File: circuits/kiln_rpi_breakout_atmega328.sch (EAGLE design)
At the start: 31 parts, among them Q1 5A, U1 INA125P

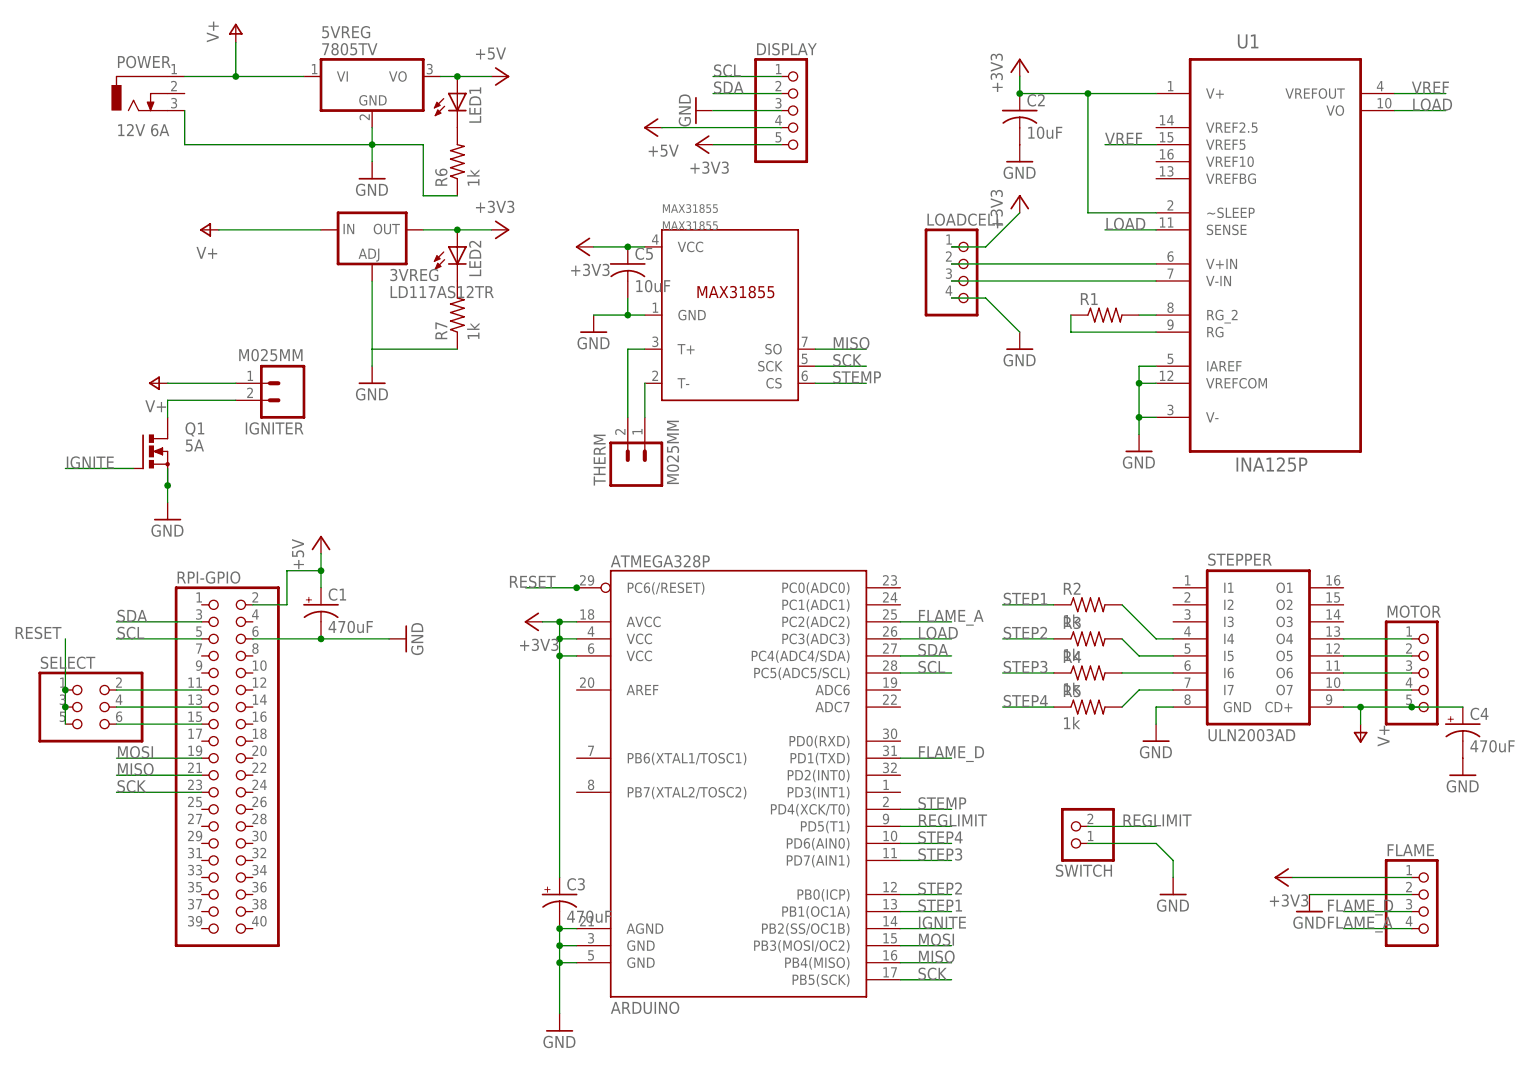
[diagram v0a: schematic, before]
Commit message: Add auxtemp header, stacking power connector
Managed to update the pcb order in time. Auxtemp header takes a DS18B20
chip as an auxiliary temperature monitor, good for checking for propane
tank freezing or even as primary temperature control. Additional
powerstack header allows stacked breakouts to pass power between boards
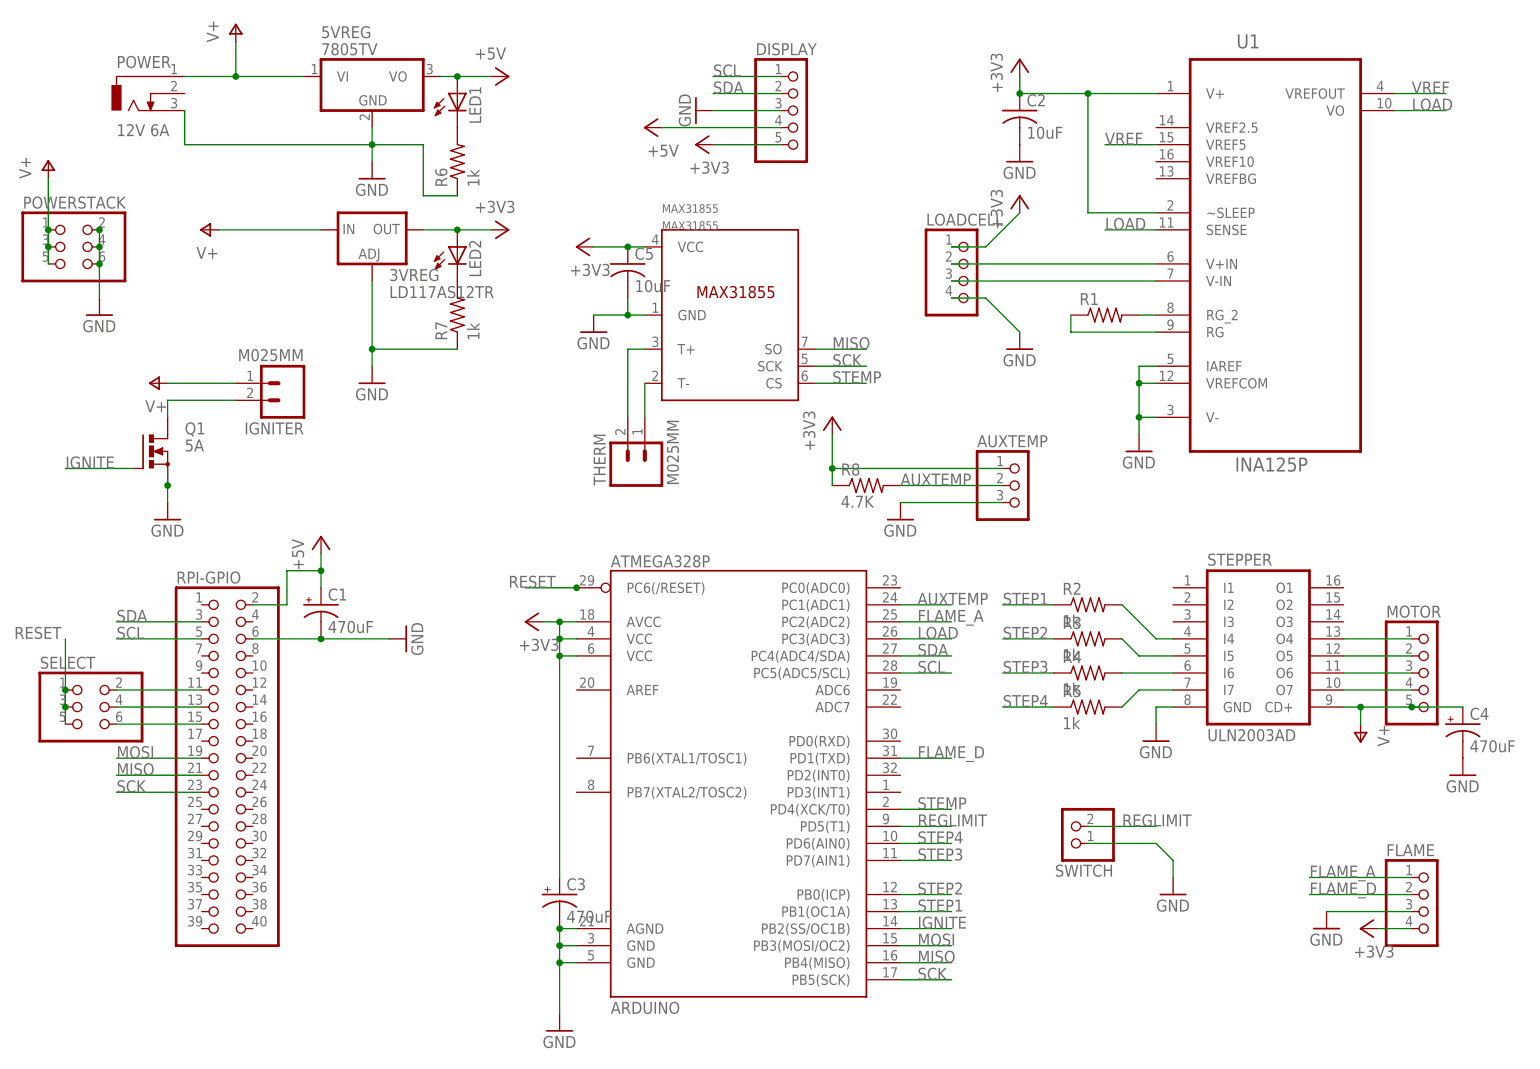
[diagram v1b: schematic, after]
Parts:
- added AUXTEMP: (no value), pinhead:PINHD-1X3
- added POWERSTACK: (no value), pinhead:PINHD-2X3
- added R8: 4.7K, rcl:R-US_0207/2V
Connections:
- new net AUXTEMP: ARDUINO.PC1(ADC1), AUXTEMP.2, R8.2
- net +3V3: now also AUXTEMP.1, FLAME.4, R8.1; no longer FLAME.1
- net FLAME_A: now also FLAME.1; no longer FLAME.4
- net FLAME_D: now also FLAME.2; no longer FLAME.3
- net GND: now also AUXTEMP.3, FLAME.3, POWERSTACK.2, POWERSTACK.4, POWERSTACK.6; no longer FLAME.2
- net V+: now also POWERSTACK.1, POWERSTACK.3, POWERSTACK.5
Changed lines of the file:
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@@
 <part name="+3V2" library="supply1" deviceset="+3V3" device=""/>
 <part name="GND9" library="supply1" deviceset="GND" device=""/>
+<part name="POWERSTACK" library="pinhead" deviceset="PINHD-2X3" device=""/>
+<part name="P+8" library="supply1" deviceset="V+" device=""/>
+<part name="GND15" library="supply1" deviceset="GND" device=""/>
+<part name="AUXTEMP" library="pinhead" deviceset="PINHD-1X3" device=""/>
+<part name="R8" library="rcl" deviceset="R-US_" device="0207/2V" value="4.7K"/>
+<part name="GND16" library="supply1" deviceset="GND" device=""/>
+<part name="+3V8" library="supply1" deviceset="+3V3" device=""/>
 </parts>
 <sheets>
@@
 <instance part="R7" gate="G$1" x="22.86" y="119.38" rot="R90"/>
 <instance part="FLAME" gate="A" x="167.64" y="30.48"/>
-<instance part="+3V2" gate="G$1" x="144.78" y="35.56" rot="R90"/>
-<instance part="GND9" gate="1" x="149.86" y="30.48"/>
+<instance part="+3V2" gate="G$1" x="157.48" y="27.94" rot="R90"/>
+<instance part="GND9" gate="1" x="152.4" y="27.94"/>
+<instance part="POWERSTACK" gate="A" x="-35.56" y="129.54"/>
+<instance part="P+8" gate="1" x="-38.1" y="142.24"/>
+<instance part="GND15" gate="1" x="-30.48" y="119.38"/>
+<instance part="AUXTEMP" gate="A" x="106.68" y="93.98"/>
+<instance part="R8" gate="G$1" x="83.82" y="93.98"/>
+<instance part="GND16" gate="1" x="88.9" y="88.9"/>
+<instance part="+3V8" gate="G$1" x="78.74" y="104.14"/>
 </instances>
 <busses>
@@
 <wire x1="10.16" y1="114.3" x2="10.16" y2="111.76" width="0.1524" layer="91"/>
 <wire x1="10.16" y1="114.3" x2="22.86" y2="114.3" width="0.1524" layer="91"/>
+<junction x="10.16" y="114.3"/>
 </segment>
 <segment>
@@
 </segment>
 <segment>
+<pinref part="POWERSTACK" gate="A" pin="2"/>
+<pinref part="GND15" gate="1" pin="GND"/>
+<wire x1="-30.48" y1="132.08" x2="-30.48" y2="129.54" width="0.1524" layer="91"/>
+<junction x="-30.48" y="132.08"/>
+<pinref part="POWERSTACK" gate="A" pin="4"/>
+<junction x="-30.48" y="129.54"/>
+<wire x1="-30.48" y1="129.54" x2="-30.48" y2="127" width="0.1524" layer="91"/>
+<pinref part="POWERSTACK" gate="A" pin="6"/>
+<junction x="-30.48" y="127"/>
+<wire x1="-30.48" y1="127" x2="-30.48" y2="121.92" width="0.1524" layer="91"/>
+</segment>
+<segment>
+<pinref part="AUXTEMP" gate="A" pin="3"/>
+<wire x1="104.14" y1="91.44" x2="88.9" y2="91.44" width="0.1524" layer="91"/>
+<pinref part="GND16" gate="1" pin="GND"/>
+</segment>
+<segment>
+<pinref part="FLAME" gate="A" pin="3"/>
 <pinref part="GND9" gate="1" pin="GND"/>
-<pinref part="FLAME" gate="A" pin="2"/>
-<wire x1="149.86" y1="33.02" x2="165.1" y2="33.02" width="0.1524" layer="91"/>
+<wire x1="165.1" y1="30.48" x2="152.4" y2="30.48" width="0.1524" layer="91"/>
 </segment>
 </net>
@@
 <pinref part="3VREG" gate="G$1" pin="IN"/>
 <wire x1="-12.7" y1="132.08" x2="2.54" y2="132.08" width="0.1524" layer="91"/>
+</segment>
+<segment>
+<pinref part="POWERSTACK" gate="A" pin="5"/>
+<pinref part="P+8" gate="1" pin="V+"/>
+<wire x1="-38.1" y1="127" x2="-38.1" y2="129.54" width="0.1524" layer="91"/>
+<pinref part="POWERSTACK" gate="A" pin="3"/>
+<junction x="-38.1" y="129.54"/>
+<wire x1="-38.1" y1="129.54" x2="-38.1" y2="132.08" width="0.1524" layer="91"/>
+<pinref part="POWERSTACK" gate="A" pin="1"/>
+<junction x="-38.1" y="132.08"/>
+<wire x1="-38.1" y1="132.08" x2="-38.1" y2="139.7" width="0.1524" layer="91"/>
 </segment>
 </net>
@@
 </segment>
 <segment>
-<pinref part="FLAME" gate="A" pin="1"/>
+<pinref part="AUXTEMP" gate="A" pin="1"/>
+<wire x1="104.14" y1="96.52" x2="78.74" y2="96.52" width="0.1524" layer="91"/>
+<pinref part="+3V8" gate="G$1" pin="+3V3"/>
+<wire x1="78.74" y1="96.52" x2="78.74" y2="101.6" width="0.1524" layer="91"/>
+<pinref part="R8" gate="G$1" pin="1"/>
+<wire x1="78.74" y1="93.98" x2="78.74" y2="96.52" width="0.1524" layer="91"/>
+<junction x="78.74" y="96.52"/>
+</segment>
+<segment>
+<pinref part="FLAME" gate="A" pin="4"/>
 <pinref part="+3V2" gate="G$1" pin="+3V3"/>
-<wire x1="165.1" y1="35.56" x2="147.32" y2="35.56" width="0.1524" layer="91"/>
+<wire x1="165.1" y1="27.94" x2="160.02" y2="27.94" width="0.1524" layer="91"/>
 </segment>
 </net>
@@
 <net name="FLAME_D" class="0">
 <segment>
-<pinref part="FLAME" gate="A" pin="3"/>
-<wire x1="165.1" y1="30.48" x2="154.94" y2="30.48" width="0.1524" layer="91"/>
-<label x="152.4" y="30.48" size="1.778" layer="95"/>
-</segment>
-<segment>
 <pinref part="ARDUINO" gate="G$1" pin="PD1(TXD)"/>
 <wire x1="88.9" y1="53.34" x2="96.52" y2="53.34" width="0.1524" layer="91"/>
 <label x="91.44" y="53.34" size="1.778" layer="95"/>
 </segment>
+<segment>
+<pinref part="FLAME" gate="A" pin="2"/>
+<wire x1="165.1" y1="33.02" x2="149.86" y2="33.02" width="0.1524" layer="91"/>
+<label x="149.86" y="33.02" size="1.778" layer="95"/>
+</segment>
 </net>
 <net name="FLAME_A" class="0">
-<segment>
-<pinref part="FLAME" gate="A" pin="4"/>
-<wire x1="165.1" y1="27.94" x2="154.94" y2="27.94" width="0.1524" layer="91"/>
-<label x="152.4" y="27.94" size="1.778" layer="95"/>
-</segment>
 <segment>
 <pinref part="ARDUINO" gate="G$1" pin="PC2(ADC2)"/>
@@
 <label x="91.44" y="73.66" size="1.778" layer="95"/>
 </segment>
+<segment>
+<pinref part="FLAME" gate="A" pin="1"/>
+<wire x1="165.1" y1="35.56" x2="149.86" y2="35.56" width="0.1524" layer="91"/>
+<label x="149.86" y="35.56" size="1.778" layer="95"/>
+</segment>
 </net>
 <net name="REGLIMIT" class="0">
@@
 </segment>
 </net>
+<net name="AUXTEMP" class="0">
+<segment>
+<pinref part="AUXTEMP" gate="A" pin="2"/>
+<wire x1="104.14" y1="93.98" x2="88.9" y2="93.98" width="0.1524" layer="91"/>
+<label x="88.9" y="93.98" size="1.778" layer="95"/>
+<pinref part="R8" gate="G$1" pin="2"/>
+</segment>
+<segment>
+<pinref part="ARDUINO" gate="G$1" pin="PC1(ADC1)"/>
+<wire x1="88.9" y1="76.2" x2="96.52" y2="76.2" width="0.1524" layer="91"/>
+<label x="91.44" y="76.2" size="1.778" layer="95"/>
+</segment>
+</net>
